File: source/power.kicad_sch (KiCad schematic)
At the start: 104 parts

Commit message: Add files via upload
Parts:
- Q3: renamed from Q?; value CSD19536KCS -> NCEP60T20
- gave numbers to parts that had none: 103

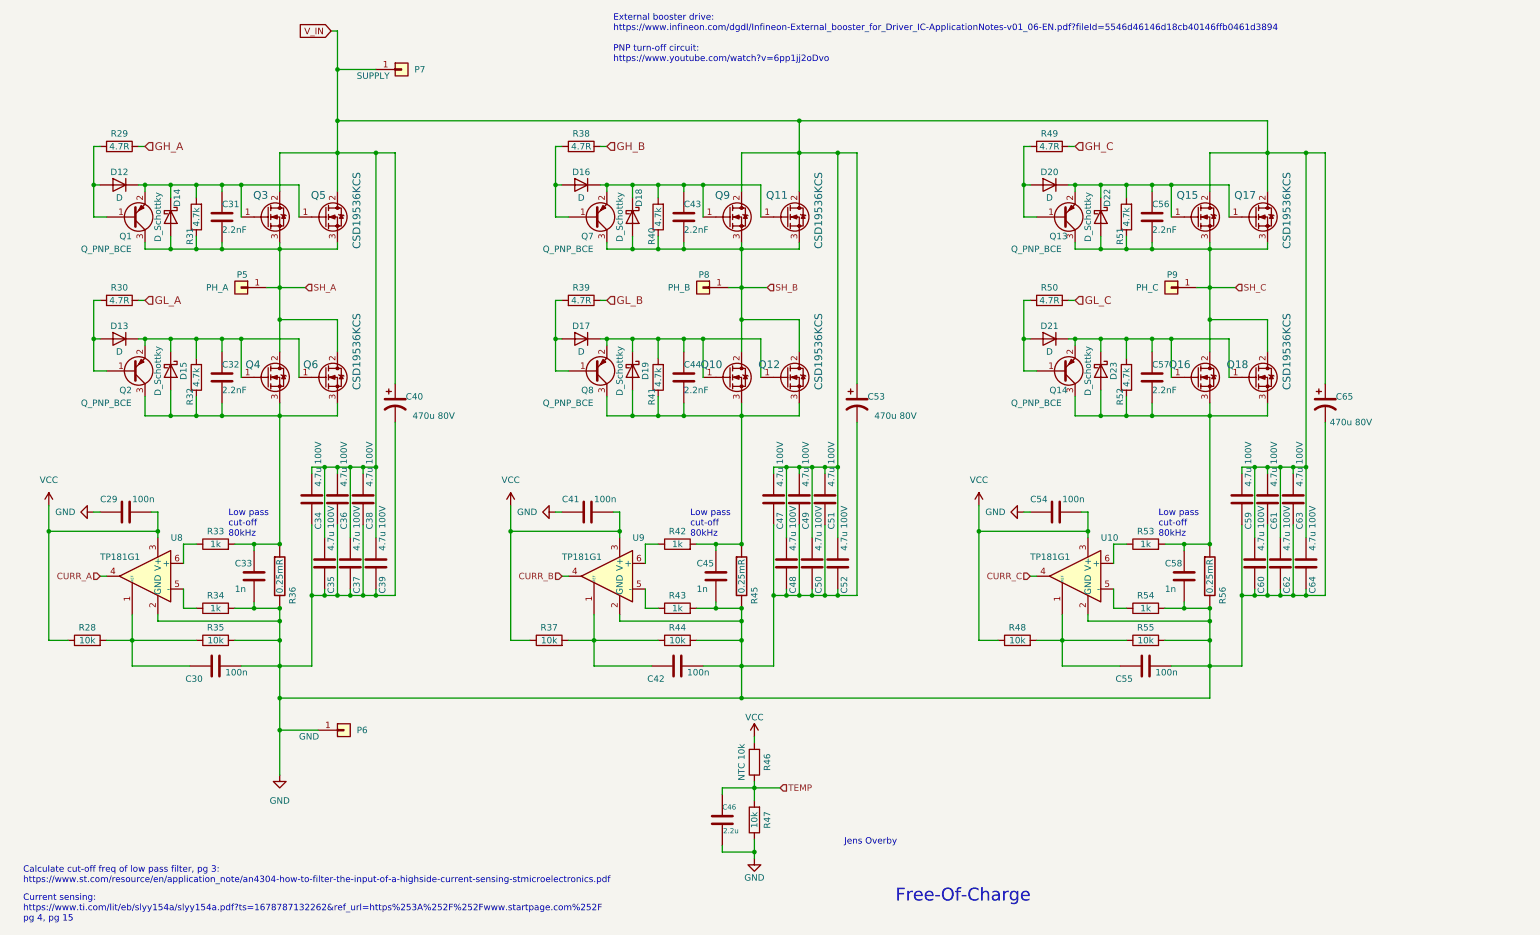
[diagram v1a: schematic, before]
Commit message: Changes suggested by mxlemming, Elwin and hackey on Discord
New power supplies and using other op-amps for current sense
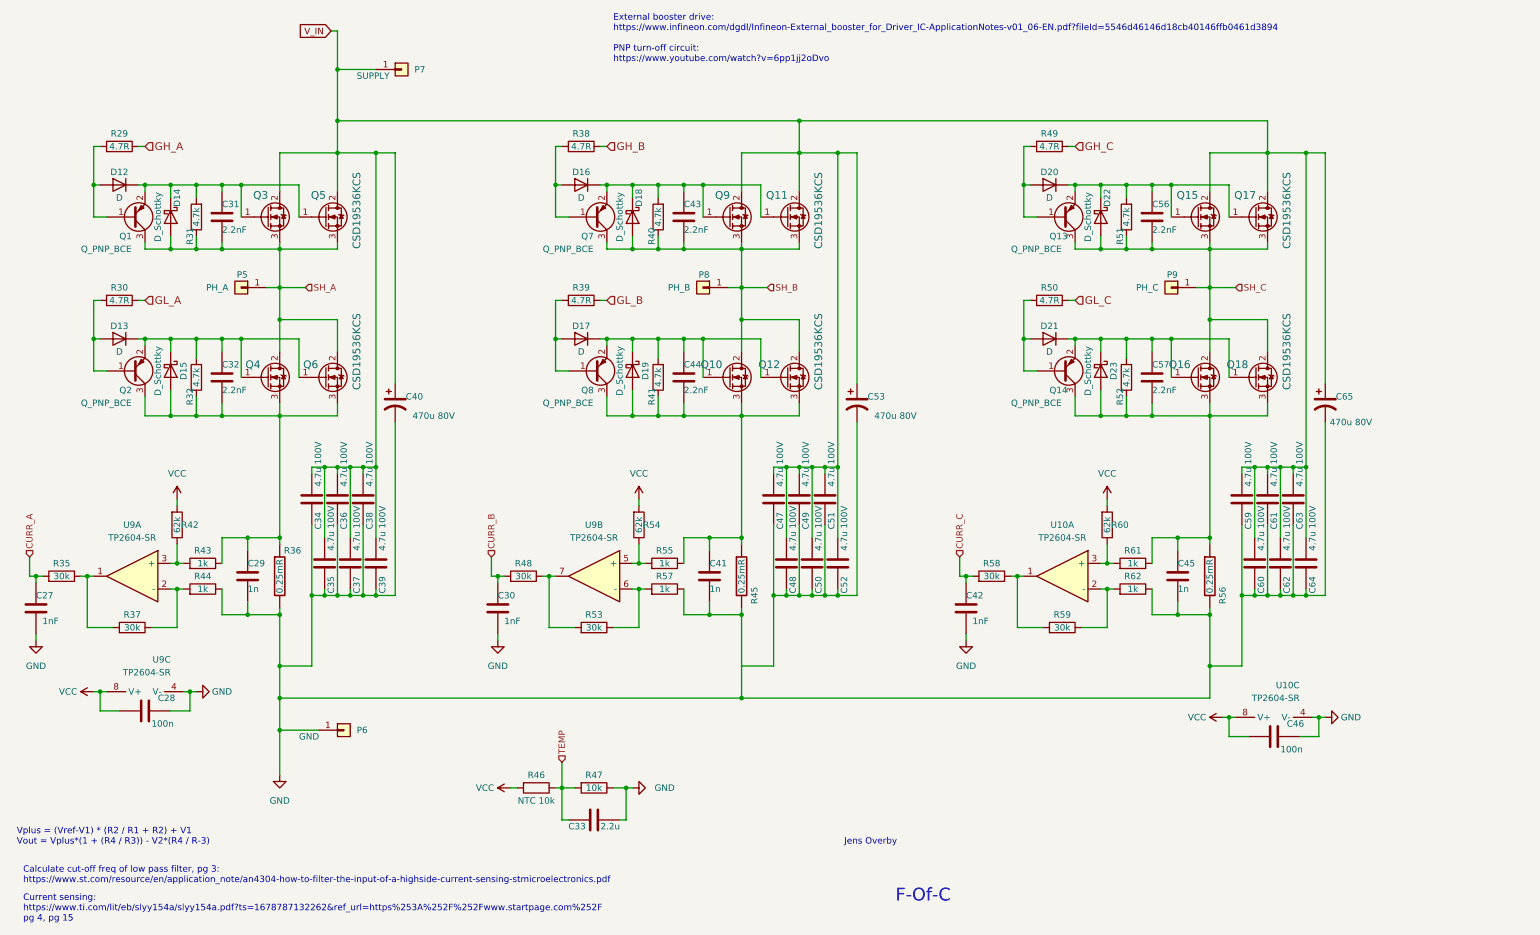
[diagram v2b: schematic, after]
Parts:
- removed C54, C55: 100n, Capacitor_SMD:C_0603_1608Metric, symbol BLDC_4-rescue:C-RESCUE-BLDC_4
- removed C58: 1n, Capacitor_SMD:C_0603_1608Metric, symbol BLDC_4-rescue:C-RESCUE-BLDC_4
- removed R28: 10k, symbol Device:R
- removed R33, R34: 1k, symbol Device:R
- removed U10, U8, U9: TP181G1, Package_TO_SOT_SMD:SOT-23-6, symbol Custom_Library:TP181G1
- added C27: 1nF, Capacitor_SMD:C_0603_1608Metric, symbol BLDC_4-rescue:C-RESCUE-BLDC_4
- added C28: 100n, Capacitor_SMD:C_0603_1608Metric, symbol BLDC_4-rescue:C-RESCUE-BLDC_4
- added R57, R61, R62: 1k, symbol Device:R
- added R58, R59: 30k, symbol Device:R
- added R60: 62k, symbol Device:R
- added U10, U9: TP2604-SR, Package_SO:SOIC-8_3.9x4.9mm_P1.27mm, symbol Custom_Library:TP2604-SR
- C29, C41: value 100n -> 1n
- C30, C42: value 100n -> 1nF
- C33: value 1n -> 2.2u
- C46: value 2.2u -> 100n
- R35, R37, R48: value 10k -> 30k
- R42, R54: value 1k -> 62k
- R44, R55: value 10k -> 1k
- R53: value 1k -> 30k
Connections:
- net CURR_A: now also R35.2, C27.2
- net CURR_B: now also C30.2, R48.2
- net CURR_C: now also C42.2, R58.2
- net GND: now also C29.1, C30.1, C33.1, C41.1, C42.1, C45.1, C46.1, R44.1, C27.1, C28.1, R57.1, R62.1, U10.4 (V-), U9.4 (V-); no longer C29.2, C30.2, C33.2, C41.2, C42.2, C45.2, C46.2, C47.1, C48.1, C49.1, C50.1, C51.1, C52.1, C53.2, R35.2, R43.2, R44.2, R54.2, R55.2
- net TEMP: now also C33.2; no longer C46.1
- net VCC: now also C46.2, R42.2, R54.2, C28.2, R60.2, U10.8 (V+), U9.8 (V+); no longer C29.1, C41.1, R37.1, R48.1
- net at R42.1: now also R43.2, U9.3 (+)
- net at C44.2, D19.2 (A), Q10.3 (S)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: now also C41.2, R55.1; no longer C45.1, R42.2
- net at R35.1: now also R37.2, U9.1; no longer C30.1
- net at C32.2, D15.2 (A), Q2.3 (C)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: now also C29.2, R43.1; no longer C33.1
- net at C57.2, D23.2 (A), Q14.3 (C)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: now also C45.2, R61.1; no longer R53.2
- net at R54.1: now also R55.2, U9.5 (+)
- net at R53.1: now also R57.2, U9.6 (-)
- new net: R37.1, R44.2, U9.2 (-)
- new net: R58.1, R59.2, U10.1
- new net: R59.1, R62.2, U10.2 (-)
- new net: C47.1, C48.1, C49.1, C50.1, C51.1, C52.1, C53.2
- new net: R48.1, R53.2, U9.7
- new net: R60.1, R61.2, U10.3 (+)
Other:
- note added: "F-Of-C"
- note added: "Vplus = (Vref-V1) * (R2 / R1 + R2) + V1 Vout = Vplus*(1 + (R4 / R3)) - V2*(R4 / R­3)"
- note removed: "Free-Of-Charge"
- note removed: "Low pass cut-off 80kHz"
- moved on the sheet: R46, R47

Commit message: First attempt of layout
It's a rats nest. Will have to remove some connections temporarily for the first prototype.
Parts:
- removed D12, D13, D16, D17, D20, D21: D, symbol Device:D
- removed D14, D15, D18, D19, D22, D23: D_Schottky, Diode_SMD:D_SOD-323, symbol Device:D_Schottky
- added C2003, C2004: 2.2u, Capacitor_SMD:C_0603_1608Metric, symbol BLDC_4-rescue:C-RESCUE-BLDC_4
- added D13, D14, D17, D18, D21, D22: 1N4148WS, Diode_SMD:D_SOD-323, symbol Diode:1N4148W
- C41: renamed from C40; footprint (none) -> Capacitor_THT:CP_Radial_D8.0mm_P5.00mm
- C53, C65: footprint (none) -> Capacitor_THT:CP_Radial_D8.0mm_P5.00mm
- P5, P6, P7, P8, P9: footprint (none) -> Connector:Banana_Jack_1Pin
- Q1, Q13, Q14, Q2, Q7, Q8: value Q_PNP_BCE -> FMMT593TA
- Q10, Q11, Q12, Q15, Q16, Q17, Q18, Q3, Q4, Q5, Q6, Q9: footprint shapes3D:TO-220-3_Horizontal_TabUp_no_hole -> Package_TO_SOT_THT:TO-220-3_Vertical
- R34: renamed from R35; footprint (none) -> Resistor_SMD:R_0402_1005Metric
- R35: renamed from R29; footprint (none) -> Resistor_SMD:R_0402_1005Metric
- R36: renamed from R30; footprint (none) -> Resistor_SMD:R_0402_1005Metric
- R37, R59, R60: footprint (none) -> Resistor_SMD:R_0402_1005Metric
- R38: renamed from R42; footprint (none) -> Resistor_SMD:R_0402_1005Metric
- R39: renamed from R31; footprint (none) -> Resistor_SMD:R_0402_1005Metric
- R40: renamed from R32; footprint (none) -> Resistor_SMD:R_0402_1005Metric
- R41: renamed from R43; footprint (none) -> Resistor_SMD:R_0402_1005Metric
- R42: renamed from R44; footprint (none) -> Resistor_SMD:R_0402_1005Metric
- R43: renamed from R36; value 0.25mR -> ASR-M-3-0.25F 0.25mR; footprint Resistor_SMD:R_0805_2012Metric -> Resistor_SMD:R_2512_6332Metric
- R44: renamed from R48; footprint (none) -> Resistor_SMD:R_0402_1005Metric
- R45: renamed from R46; footprint (none) -> Resistor_SMD:R_0603_1608Metric
- R46: renamed from R38; footprint (none) -> Resistor_SMD:R_0402_1005Metric
- R47: renamed from R39; footprint (none) -> Resistor_SMD:R_0402_1005Metric
- R48: renamed from R53; footprint (none) -> Resistor_SMD:R_0402_1005Metric
- R49: renamed from R47; footprint (none) -> Resistor_SMD:R_0402_1005Metric
- R50: renamed from R54; footprint (none) -> Resistor_SMD:R_0402_1005Metric
- R51: renamed from R40; footprint (none) -> Resistor_SMD:R_0402_1005Metric
- R52: renamed from R41; footprint (none) -> Resistor_SMD:R_0402_1005Metric
- R53: renamed from R55; footprint (none) -> Resistor_SMD:R_0402_1005Metric
- R54: renamed from R57; footprint (none) -> Resistor_SMD:R_0402_1005Metric
- R55: renamed from R45; value 0.25mR -> ASR-M-3-0.25F 0.25mR; footprint Resistor_SMD:R_0805_2012Metric -> Resistor_SMD:R_2512_6332Metric
- R56: renamed from R58; footprint (none) -> Resistor_SMD:R_0402_1005Metric
- R57: renamed from R49; footprint (none) -> Resistor_SMD:R_0402_1005Metric
- R58: renamed from R50; footprint (none) -> Resistor_SMD:R_0402_1005Metric
- R61: renamed from R51; footprint (none) -> Resistor_SMD:R_0402_1005Metric
- R62: renamed from R52; footprint (none) -> Resistor_SMD:R_0402_1005Metric
- R63: renamed from R61; footprint (none) -> Resistor_SMD:R_0402_1005Metric
- R64: renamed from R62; footprint (none) -> Resistor_SMD:R_0402_1005Metric
- R65: renamed from R56; value 0.25mR -> ASR-M-3-0.25F 0.25mR; footprint Resistor_SMD:R_0805_2012Metric -> Resistor_SMD:R_2512_6332Metric
- renumbered C27 to C30, C28 to C31, C31 to C32, C32 to C33, C29 to C34, C34 to C35, C35 to C36, C36 to C37, C37 to C38, C38 to C39, C39 to C40, C30 to C42, C33 to C43, C43 to C44, C44 to C45, C41 to C46, C42 to C54, C56 to C55, C57 to C56, C45 to C57, C59 to C58, C60 to C59, C61 to C60, C46 to C61
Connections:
- net GND: now also C47.1, C48.1, C49.1, C50.1, C51.1, C52.1, C53.2, C2003.1, C2004.1
- net VCC: now also C2003.2, C2004.2
- net at C56.1, Q14.2 (E), Q16.1 (G)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: now also D22.1 (K)
- net at Q14.1 (B), R58.2: now also D22.2 (A)
- net at C33.1, Q2.2 (E), Q4.1 (G)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: now also D14.1 (K)
- net at Q7.1 (B), R46.2: now also D17.2 (A)
- net at C44.1, Q11.1 (G), Q7.2 (E)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: now also D17.1 (K)
- net at C32.1, Q1.2 (E), Q3.1 (G)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: now also D13.1 (K)
- net at C45.1, Q10.1 (G), Q12.1 (G)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: now also D18.1 (K)
- net at Q1.1 (B), R35.2: now also D13.2 (A)
- net at Q8.1 (B), R47.2: now also D18.2 (A)
- net at C55.1, Q13.2 (E), Q15.1 (G)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: now also D21.1 (K)
- net at Q2.1 (B), R36.2: now also D14.2 (A)
- net at Q13.1 (B), R57.2: now also D21.2 (A)
